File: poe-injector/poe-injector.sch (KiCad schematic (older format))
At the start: 41 parts, among them IC1 ATTINY44-SS, J1 AVRISP6, Q1 ZXMP10A17E6, Q2 2N7002K, Q3 ZXMP10A17E6, Q4 2N7002K, U2 LTC6101, U4 LTC6101

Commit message: Switch to different high-side switch with better footprint; re-layout everything.
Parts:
- removed Q1, Q3: ZXMP10A17E6, ZXMP10A17E6, symbol ZXMP10A17E6
- added Q1, Q3: SQ2361EES, SOT23, symbol SQ2361EES
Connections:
- wire segments 106 -> 87
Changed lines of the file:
@@
-EESchema Schematic File Version 2  date 2/6/2013 9:15:11 PM
+EESchema Schematic File Version 2  date 2/6/2013 11:11:33 PM
 LIBS:power
 LIBS:device
@@
 $EndDescr
 $Comp
-L +5V #PWR12
+L GND #PWR?
+U 1 1 51132971
+P 5900 7550
+F 0 "#PWR?" H 5900 7550 30  0001 C CNN
+F 1 "GND" H 5900 7480 30  0001 C CNN
+	1    5900 7550
+	1    0    0    -1
+$EndComp
+$Comp
+L SQ2361EES Q3
+U 1 1 51132112
+P 6700 3800
+F 0 "Q3" H 6500 3800 50  0000 L BNN
+F 1 "SQ2361EES" H 6500 4000 50  0000 L BNN
+F 2 "SOT23" H 6700 3950 50  0001 C CNN
+	1    6700 3800
+	0    -1   -1   0
+$EndComp
+$Comp
+L SQ2361EES Q1
+U 1 1 511320FF
+P 6250 1450
+F 0 "Q1" H 6050 1450 50  0000 L BNN
+F 1 "SQ2361EES" H 6050 1650 50  0000 L BNN
+F 2 "SOT23" H 6250 1600 50  0001 C CNN
+	1    6250 1450
+	0    -1   -1   0
+$EndComp
+$Comp
+L +5V #PWR05
 U 1 1 5112C4D3
 P 5150 4050
-F 0 "#PWR12" H 5150 4140 20  0001 C CNN
+F 0 "#PWR05" H 5150 4140 20  0001 C CNN
 F 1 "+5V" H 5150 4140 30  0000 C CNN
 	1    5150 4050
@@
 $EndComp
 $Comp
-L GND #PWR9
+L GND #PWR06
 U 1 1 5112C4CE
 P 4650 4550
-F 0 "#PWR9" H 4650 4550 30  0001 C CNN
+F 0 "#PWR06" H 4650 4550 30  0001 C CNN
 F 1 "GND" H 4650 4480 30  0001 C CNN
 	1    4650 4550
@@
 Connection ~ 5800 3600
 Wire Wire Line
-	6600 3600 6550 3600
-Wire Wire Line
-	6550 3600 6500 3600
-Wire Wire Line
-	6500 3600 6450 3600
-Wire Wire Line
-	6450 3600 5800 3600
-Wire Wire Line
-	5800 3600 5700 3600
+	6600 3600 5700 3600
 Wire Wire Line
 	8300 2700 8300 2500
@@
 	8300 2500 7800 2500
 Wire Wire Line
-	5900 7550 5900 7450
-Wire Wire Line
-	5900 7450 5900 7250
+	5900 7550 5900 7250
 Wire Wire Line
 	900  2450 900  3850
@@
 Connection ~ 6400 1750
 Wire Wire Line
-	6500 1750 6400 1750
-Wire Wire Line
-	6400 1750 6350 1750
+	6500 1750 6350 1750
 Wire Wire Line
 	5300 1850 5300 2450
@@
 	7800 1750 7800 2300
 Wire Wire Line
-	6350 1250 6500 1250
-Wire Wire Line
-	6500 1250 7100 1250
-Wire Wire Line
-	7100 1250 7200 1250
-Connection ~ 6100 1250
-Connection ~ 6050 1250
-Connection ~ 6000 1250
+	6350 1250 7200 1250
 Wire Wire Line
 	7700 1250 8700 1250
@@
 	7550 3600 7550 4650
 Wire Wire Line
-	8800 3600 8500 3600
-Wire Wire Line
-	8500 3600 8150 3600
-Connection ~ 6450 3600
-Connection ~ 6500 3600
-Connection ~ 6550 3600
-Wire Wire Line
-	6800 3600 6950 3600
-Wire Wire Line
-	6950 3600 7550 3600
-Wire Wire Line
-	7550 3600 7650 3600
+	8800 3600 8150 3600
+Wire Wire Line
+	6800 3600 7650 3600
 Wire Wire Line
 	6800 4000 6800 4100
@@
 	5600 2450 5600 1850
 Wire Wire Line
-	6800 4100 6850 4100
-Wire Wire Line
-	6850 4100 6950 4100
+	6800 4100 6950 4100
 Connection ~ 6850 4100
 Wire Wire Line
@@
 	5900 4800 5900 4200
 Wire Wire Line
-	5800 4800 5800 4200
-Wire Wire Line
-	5800 4200 5800 4150
+	5800 4800 5800 4150
 Connection ~ 5800 4200
 Wire Wire Line
@@
 	5200 4200 5200 3600
 Wire Wire Line
-	5200 3600 5400 3600
-Wire Wire Line
-	5400 3600 5500 3600
+	5200 3600 5500 3600
 Connection ~ 5400 3600
 Wire Wire Line
-	5200 1250 5100 1250
-Wire Wire Line
-	5100 1250 4900 1250
+	5200 1250 4900 1250
 Wire Wire Line
 	4900 1250 4900 1850
@@
 	8750 4850 8750 5050
 Wire Wire Line
-	6150 1250 6100 1250
-Wire Wire Line
-	6100 1250 6050 1250
-Wire Wire Line
-	6050 1250 6000 1250
-Wire Wire Line
-	6000 1250 5500 1250
-Wire Wire Line
-	5500 1250 5400 1250
+	6150 1250 5400 1250
 Connection ~ 5500 1250
 Wire Wire Line
@@
 $EndComp
 $Comp
-L GND #PWR8
+L GND #PWR07
 U 1 1 5112C48D
 P 4050 3050
-F 0 "#PWR8" H 4050 3050 30  0001 C CNN
+F 0 "#PWR07" H 4050 3050 30  0001 C CNN
 F 1 "GND" H 4050 2980 30  0001 C CNN
 	1    4050 3050
@@
 $EndComp
 $Comp
-L +5V #PWR7
+L +5V #PWR08
 U 1 1 5112C0CC
 P 3550 2550
-F 0 "#PWR7" H 3550 2640 20  0001 C CNN
+F 0 "#PWR08" H 3550 2640 20  0001 C CNN
 F 1 "+5V" H 3550 2640 30  0000 C CNN
 	1    3550 2550
@@
 $EndComp
 $Comp
-L +5V #PWR5
+L +5V #PWR09
 U 1 1 5111AFF4
 P 2050 1050
-F 0 "#PWR5" H 2050 1140 20  0001 C CNN
+F 0 "#PWR09" H 2050 1140 20  0001 C CNN
 F 1 "+5V" H 2050 1140 30  0000 C CNN
 	1    2050 1050
@@
 $EndComp
 $Comp
-L GND #PWR6
+L GND #PWR010
 U 1 1 5111AFED
 P 2050 1450
-F 0 "#PWR6" H 2050 1450 30  0001 C CNN
+F 0 "#PWR010" H 2050 1450 30  0001 C CNN
 F 1 "GND" H 2050 1380 30  0001 C CNN
 	1    2050 1450
@@
 $EndComp
 $Comp
-L VPP #PWR25
+L VPP #PWR27
 U 1 1 511185E5
 P 9450 1800
-F 0 "#PWR25" H 9450 2000 40  0001 C CNN
+F 0 "#PWR27" H 9450 2000 40  0001 C CNN
 F 1 "VPP" H 9450 1950 40  0000 C CNN
 	1    9450 1800
@@
 $EndComp
 $Comp
-L +48V #PWR24
+L +48V #PWR011
 U 1 1 511185CE
 P 9450 1300
-F 0 "#PWR24" H 9450 1430 20  0001 C CNN
+F 0 "#PWR011" H 9450 1430 20  0001 C CNN
 F 1 "+48V" H 9450 1400 30  0000 C CNN
 	1    9450 1300
@@
 $EndComp
 $Comp
-L +48V #PWR19
+L +48V #PWR012
 U 1 1 5111849B
 P 7550 5050
-F 0 "#PWR19" H 7550 5180 20  0001 C CNN
+F 0 "#PWR012" H 7550 5180 20  0001 C CNN
 F 1 "+48V" H 7550 5150 30  0000 C CNN
 	1    7550 5050
@@
 $EndComp
 $Comp
-L +48V #PWR18
+L +48V #PWR013
 U 1 1 51118493
 P 7100 2700
-F 0 "#PWR18" H 7100 2830 20  0001 C CNN
+F 0 "#PWR013" H 7100 2830 20  0001 C CNN
 F 1 "+48V" H 7100 2800 30  0000 C CNN
 	1    7100 2700
@@
 $EndComp
 $Comp
-L +48V #PWR21
+L +48V #PWR014
 U 1 1 51118467
 P 8700 1250
-F 0 "#PWR21" H 8700 1380 20  0001 C CNN
+F 0 "#PWR014" H 8700 1380 20  0001 C CNN
 F 1 "+48V" H 8700 1350 30  0000 C CNN
 	1    8700 1250
@@
 $EndComp
 $Comp
-L VPP #PWR16
+L VPP #PWR18
 U 1 1 5111840D
 P 6550 2750
-F 0 "#PWR16" H 6550 2950 40  0001 C CNN
+F 0 "#PWR18" H 6550 2950 40  0001 C CNN
 F 1 "VPP" H 6550 2900 40  0000 C CNN
 	1    6550 2750
@@
 $EndComp
 $Comp
-L VPP #PWR17
+L VPP #PWR19
 U 1 1 51118403
 P 7000 5100
-F 0 "#PWR17" H 7000 5300 40  0001 C CNN
+F 0 "#PWR19" H 7000 5300 40  0001 C CNN
 F 1 "VPP" H 7000 5250 40  0000 C CNN
 	1    7000 5100
@@
 $EndComp
 $Comp
-L GND #PWR15
-U 1 1 511182B8
-P 5900 7550
-F 0 "#PWR15" H 5900 7550 30  0001 C CNN
-F 1 "GND" H 5900 7480 30  0001 C CNN
-	1    5900 7550
-	1    0    0    -1
-$EndComp
-$Comp
-L GND #PWR26
+L GND #PWR015
 U 1 1 51118117
 P 9450 2300
-F 0 "#PWR26" H 9450 2300 30  0001 C CNN
+F 0 "#PWR015" H 9450 2300 30  0001 C CNN
 F 1 "GND" H 9450 2230 30  0001 C CNN
 	1    9450 2300
@@
 $EndComp
 $Comp
-L GND #PWR4
+L GND #PWR016
 U 1 1 51117B98
 P 1500 4550
-F 0 "#PWR4" H 1500 4550 30  0001 C CNN
+F 0 "#PWR016" H 1500 4550 30  0001 C CNN
 F 1 "GND" H 1500 4480 30  0001 C CNN
 	1    1500 4550
@@
 $EndComp
 $Comp
-L +5V #PWR3
+L +5V #PWR017
 U 1 1 51117B3E
 P 1500 3350
-F 0 "#PWR3" H 1500 3440 20  0001 C CNN
+F 0 "#PWR017" H 1500 3440 20  0001 C CNN
 F 1 "+5V" H 1500 3440 30  0000 C CNN
 	1    1500 3350
@@
 $EndComp
 $Comp
-L GND #PWR20
+L GND #PWR018
 U 1 1 5111744B
 P 8300 2700
-F 0 "#PWR20" H 8300 2700 30  0001 C CNN
+F 0 "#PWR018" H 8300 2700 30  0001 C CNN
 F 1 "GND" H 8300 2630 30  0001 C CNN
 	1    8300 2700
@@
 $EndComp
 $Comp
-L GND #PWR22
+L GND #PWR019
 U 1 1 51117447
 P 8750 5050
-F 0 "#PWR22" H 8750 5050 30  0001 C CNN
+F 0 "#PWR019" H 8750 5050 30  0001 C CNN
 F 1 "GND" H 8750 4980 30  0001 C CNN
 	1    8750 5050
@@
 $EndComp
 $Comp
-L GND #PWR10
+L GND #PWR020
 U 1 1 511083A8
 P 4900 1850
-F 0 "#PWR10" H 4900 1850 30  0001 C CNN
+F 0 "#PWR020" H 4900 1850 30  0001 C CNN
 F 1 "GND" H 4900 1780 30  0001 C CNN
 	1    4900 1850
@@
 $EndComp
 $Comp
-L GND #PWR14
+L GND #PWR021
 U 1 1 5110833F
 P 5200 4800
-F 0 "#PWR14" H 5200 4800 30  0001 C CNN
+F 0 "#PWR021" H 5200 4800 30  0001 C CNN
 F 1 "GND" H 5200 4730 30  0001 C CNN
 	1    5200 4800
@@
 $EndComp
 $Comp
-L +48V #PWR23
+L +48V #PWR022
 U 1 1 51106F2B
 P 8800 3600
-F 0 "#PWR23" H 8800 3730 20  0001 C CNN
+F 0 "#PWR022" H 8800 3730 20  0001 C CNN
 F 1 "+48V" H 8800 3700 30  0000 C CNN
 	1    8800 3600
@@
 $EndComp
 $Comp
-L GND #PWR11
+L GND #PWR023
 U 1 1 51105C25
 P 4900 2450
-F 0 "#PWR11" H 4900 2450 30  0001 C CNN
+F 0 "#PWR023" H 4900 2450 30  0001 C CNN
 F 1 "GND" H 4900 2380 30  0001 C CNN
 	1    4900 2450
@@
 $EndComp
 $Comp
-L GND #PWR13
+L GND #PWR024
 U 1 1 51105BDE
 P 5200 4200
-F 0 "#PWR13" H 5200 4200 30  0001 C CNN
+F 0 "#PWR024" H 5200 4200 30  0001 C CNN
 F 1 "GND" H 5200 4130 30  0001 C CNN
 	1    5200 4200
@@
 $EndComp
 $Comp
-L ZXMP10A17E6 Q?
-U 1 1 510E9ADD
-P 6700 3800
-AR Path="/510D287D" Ref="Q?"  Part="1"
-AR Path="/510E9ADD" Ref="Q3"  Part="1"
-F 0 "Q3" H 6250 3900 50  0000 L BNN
-F 1 "ZXMP10A17E6" H 6250 3800 50  0000 L BNN
-F 2 "ZXMP10A17E6" V 6700 3950 50  0001 C CNN
-	1    6700 3800
-	0    -1   -1   0
-$EndComp
-$Comp
 L CONN_1 VBUS1
 U 1 1 510E9ADC
@@
 $EndComp
 $Comp
-L GND #PWR2
+L GND #PWR025
 U 1 1 510E9A8D
 P 1100 1350
-F 0 "#PWR2" H 1100 1350 30  0001 C CNN
+F 0 "#PWR025" H 1100 1350 30  0001 C CNN
 F 1 "GND" H 1100 1280 30  0001 C CNN
 	1    1100 1350
@@
 $EndComp
 $Comp
-L +5V #PWR1
+L +5V #PWR026
 U 1 1 510E9A89
 P 900 1350
-F 0 "#PWR1" H 900 1440 20  0001 C CNN
+F 0 "#PWR026" H 900 1440 20  0001 C CNN
 F 1 "+5V" H 900 1440 30  0000 C CNN
 	1    900  1350
@@
 $EndComp
 $Comp
-L ZXMP10A17E6 Q1
-U 1 1 510D287D
-P 6250 1450
-F 0 "Q1" H 5800 1550 50  0000 L BNN
-F 1 "ZXMP10A17E6" H 5800 1450 50  0000 L BNN
-F 2 "ZXMP10A17E6" V 6250 1600 50  0001 C CNN
-	1    6250 1450
-	0    -1   -1   0
-$EndComp
-$Comp

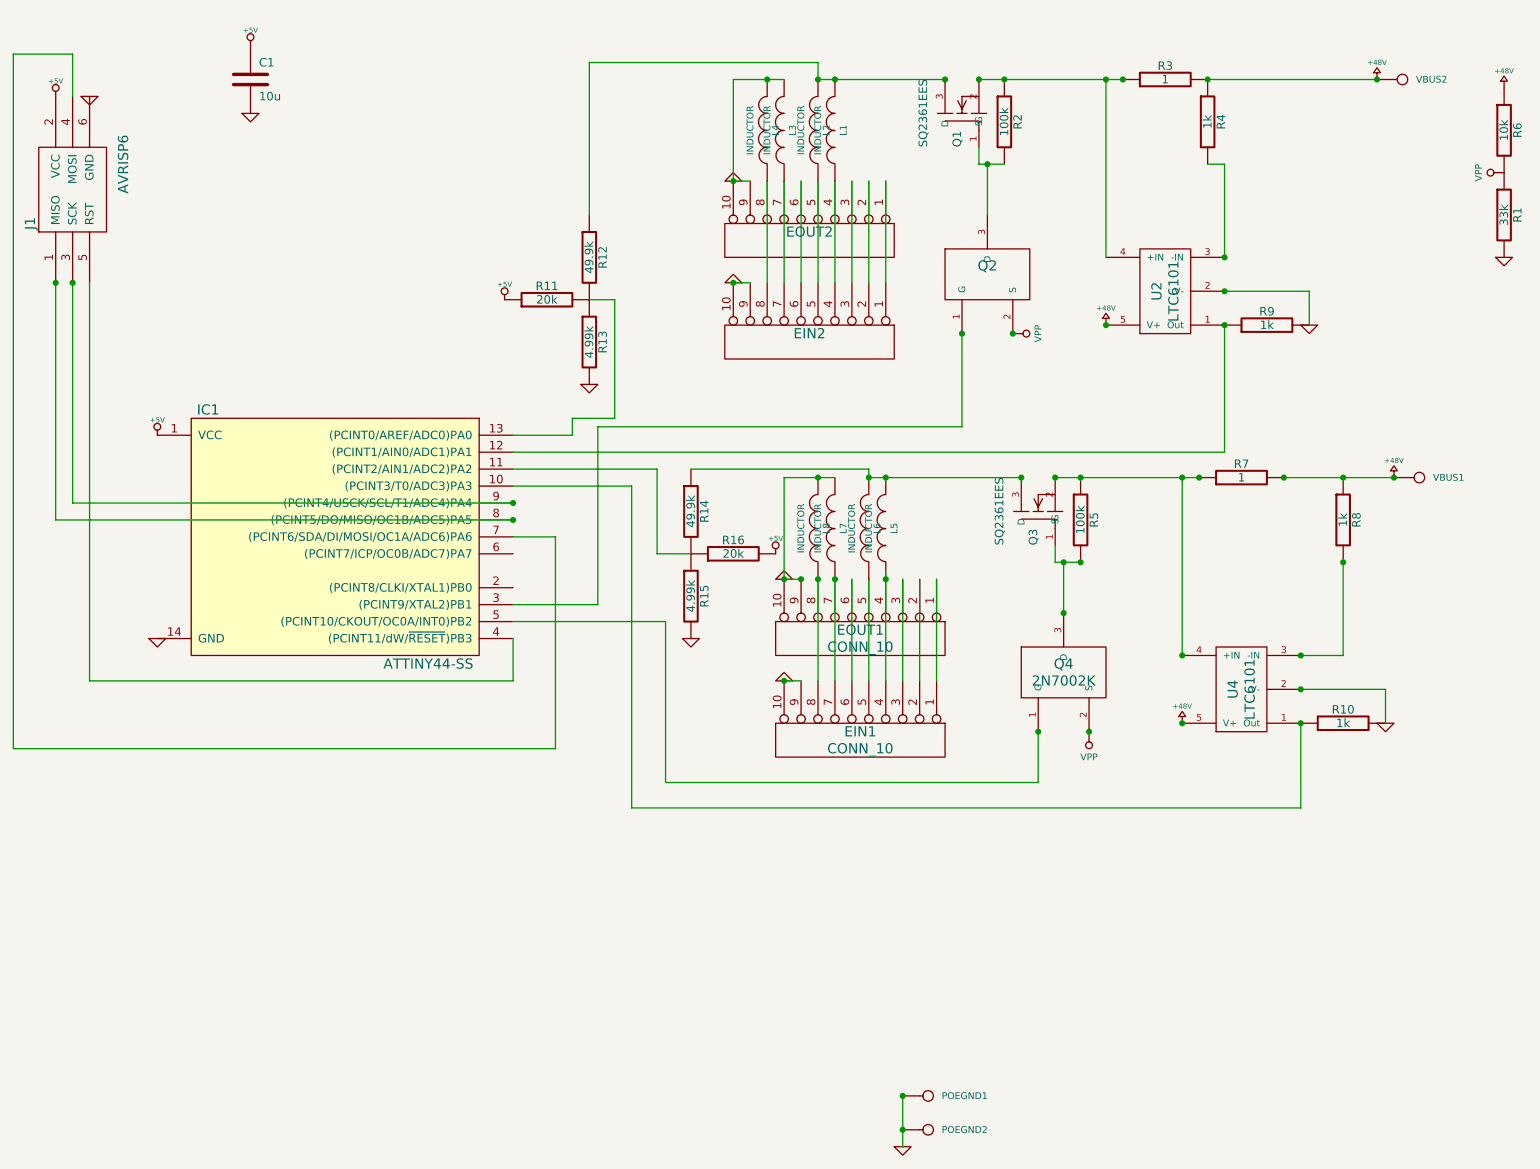
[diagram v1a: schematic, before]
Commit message: Use alternative footprint for Ethernet connector, and update project file to use the libs
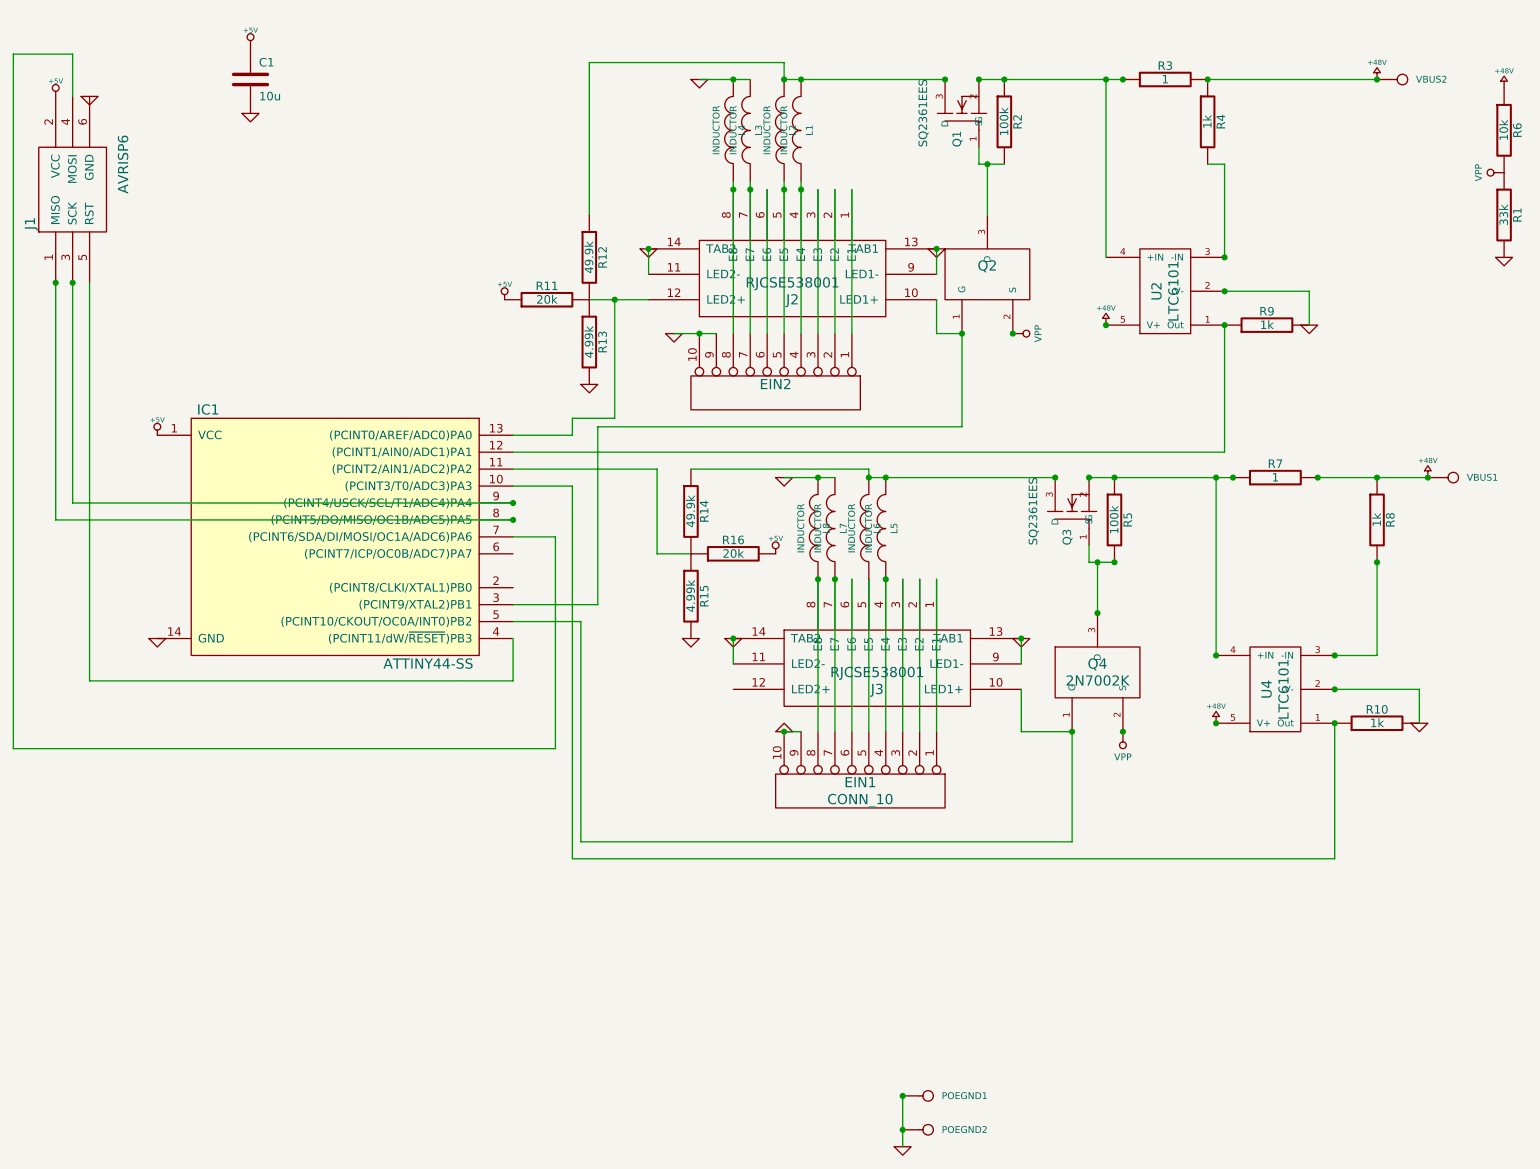
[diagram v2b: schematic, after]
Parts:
- removed EOUT1, EOUT2: CONN_10, symbol CONN_10
- added J2, J3: RJCSE538001, symbol RJCSE538001
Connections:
- net GND: now also J2.11 (LED2-), J2.13 (TAB1), J2.14 (TAB2), J2.9 (LED1-), J3.11 (LED2-), J3.13 (TAB1), J3.14 (TAB2), J3.9 (LED1-)
- net at IC1.3 ((PCINT9/XTAL2)PB1), Q2.1 (G): now also J2.10 (LED1+)
- net at IC1.5 ((PCINT10/CKOUT/OC0A/INT0)PB2), Q4.1 (G): now also J3.10 (LED1+)
- net at EIN1.1 (P1): now also J3.1 (E1)
- net at EIN1.2 (P2): now also J3.2 (E2)
- net at EIN1.3 (P3): now also J3.3 (E3)
- net at EIN1.4 (P4), L5.1: now also J3.4 (E4)
- net at EIN1.5 (P5), L6.1: now also J3.5 (E5)
- net at EIN1.6 (P6): now also J3.6 (E6)
- net at EIN1.7 (P7), L7.1: now also J3.7 (E7)
- net at EIN1.8 (P8), L8.1: now also J3.8 (E8)
- net at EIN2.1 (P1): now also J2.1 (E1)
- net at EIN2.2 (P2): now also J2.2 (E2)
- net at EIN2.3 (P3): now also J2.3 (E3)
- net at EIN2.4 (P4), L1.1: now also J2.4 (E4)
- net at EIN2.5 (P5), L2.1: now also J2.5 (E5)
- net at EIN2.6 (P6): now also J2.6 (E6)
- net at EIN2.7 (P7), L3.1: now also J2.7 (E7)
- net at EIN2.8 (P8), L4.1: now also J2.8 (E8)
- net at IC1.13 ((PCINT0/AREF/ADC0)PA0), R11.2, R12.2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: now also J2.12 (LED2+)
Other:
- moved on the sheet: EIN1, EIN2, L1, L2, L3, L4, Q3, Q4, R10, R5, R7, R8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

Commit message: Update design to make N-channel FET pull P-channel FET down properly
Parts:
- R1: value 33k -> 392K
- R6: value 10k -> 392K
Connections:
- net +48V: no longer R6.1
- net GND: now also Q2.2 (S), Q4.2 (S); no longer R1.2
- net at Q1.1 (G), R2.2: now also R1.1; no longer Q2.3 (D)
- net at Q3.1 (G), R5.2: now also R6.1; no longer Q4.3 (D)
- net at IC1.13 ((PCINT0/AREF/ADC0)PA0), R11.2, R12.2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: no longer J2.12 (LED2+)
- net at IC1.2 ((PCINT8/CLKI/XTAL1)PB0): now also J3.12 (LED2+)
- net at IC1.6 ((PCINT7/ICP/OC0B/ADC7)PA7): now also J2.12 (LED2+)
- removed net VPP: Q2.2 (S), Q4.2 (S), R1.1, R6.2
- new net: Q2.3 (D), R1.2
- new net: Q4.3 (D), R6.2
